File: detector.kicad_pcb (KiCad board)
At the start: 2 copper layers, 45 x 45 mm, 27 parts, among them J1 RF_IN_1, J2 DET_OUT_1, J3 RF_IN_2, J4 DET_OUT_2, P1 4.7k, P2 4.7k

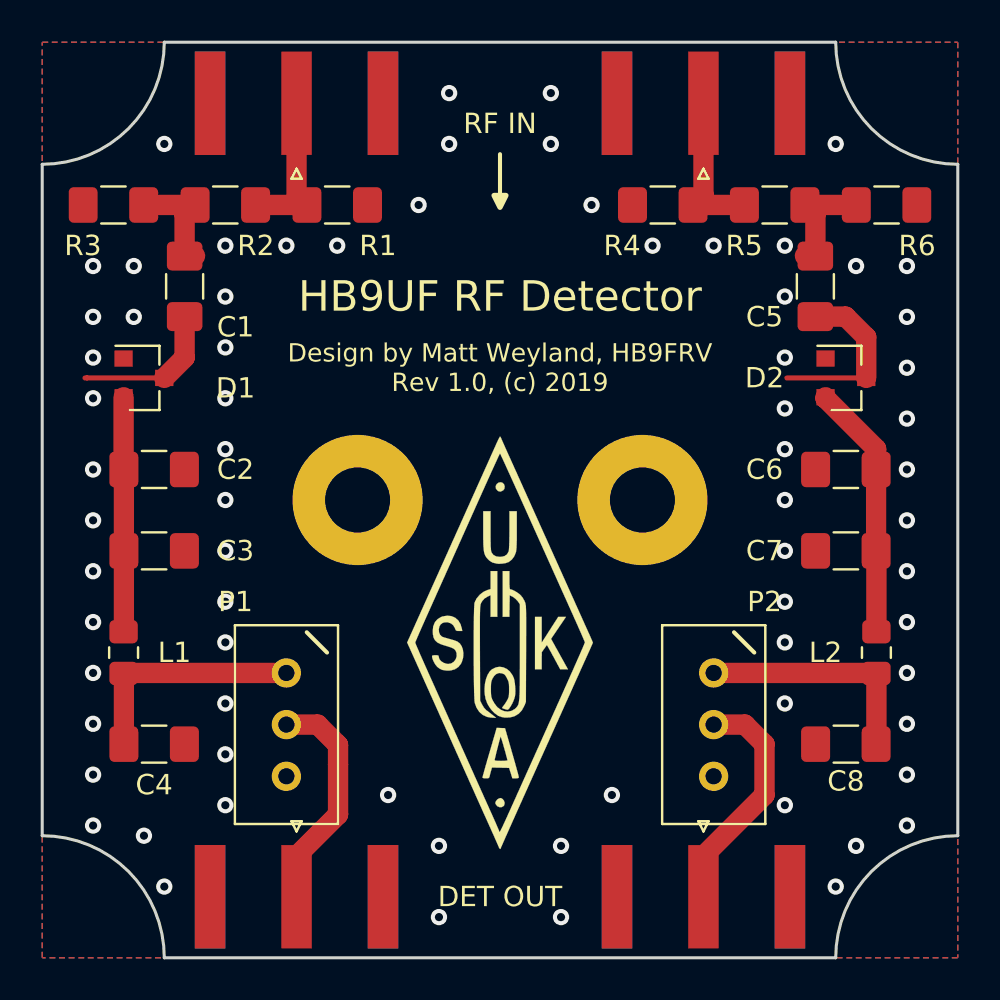
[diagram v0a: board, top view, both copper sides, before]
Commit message: Reduce size of PCB to fit in RND 455-00853 case with new footprints
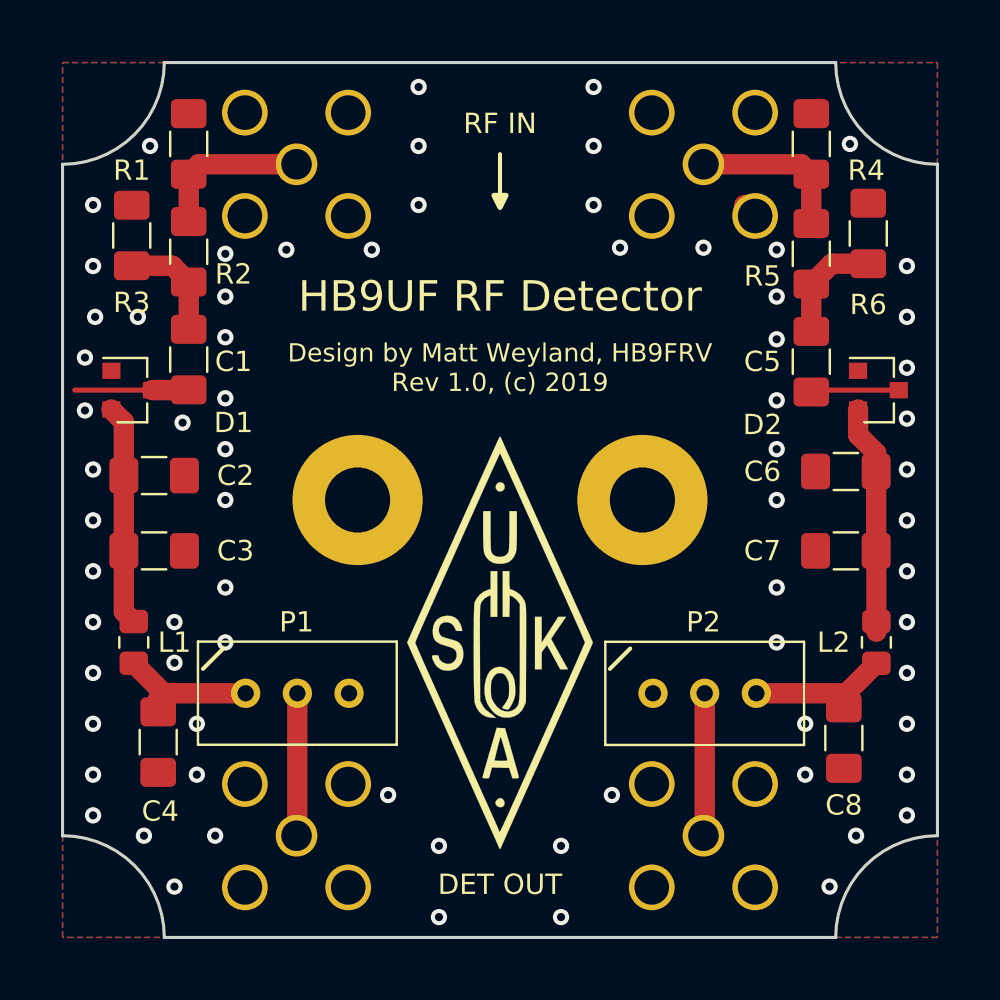
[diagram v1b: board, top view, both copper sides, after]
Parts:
- J1, J2, J3, J4: footprint Connector_Coaxial:SMA_Amphenol_132289_EdgeMount -> Connector_Coaxial:SMA_Amphenol_901-144_Vertical; moved to B.Cu
- moved R4 7.89 mm to (137.8, 55.0), turned to 90 degrees
- moved R1 7.89 mm to (107.2, 55.0), turned to 90 degrees
- moved C5 3.71 mm to (137.8, 65.7)
- moved C1 3.61 mm to (107.2, 65.6)
- moved R5 3.00 mm to (137.8, 60.4), turned to 90 degrees
- moved J1 3.00 mm to (112.5, 56.0), turned to 270 degrees
- moved J2 3.00 mm to (112.5, 89.0), turned to 90 degrees
- moved J3 3.00 mm to (132.5, 56.0), turned to 270 degrees
- moved J4 3.00 mm to (132.5, 89.0), turned to 90 degrees
- moved R2 2.92 mm to (107.2, 60.3), turned to 90 degrees
- moved P2 2.33 mm to (135.1, 82.0), turned to 0 degrees
- moved P1 2.24 mm to (110.0, 82.0), turned to 180 degrees
- moved R3 1.75 mm to (104.4, 59.5), turned to 90 degrees
- moved D2 1.71 mm to (141.1, 67.1)
- moved R6 1.66 mm to (140.6, 59.4), turned to 90 degrees
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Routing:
- net Net-(C5-Pad1): track 8.82 -> 3.90 mm
- net Net-(J4-Pad1): track 11.6 -> 7.02 mm
- net Net-(C4-Pad1): track 11.5 -> 7.24 mm
- net Net-(J2-Pad1): track 11.3 -> 7.02 mm
- net Net-(C8-Pad1): track 11.5 -> 7.28 mm
- net Net-(C1-Pad1): track 7.33 -> 5.61 mm
- net Net-(C6-Pad1): track 12.6 -> 11.4 mm
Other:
- board size 45 x 45 mm -> 43 x 43 mm
